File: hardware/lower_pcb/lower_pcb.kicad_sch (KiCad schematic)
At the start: 0 parts

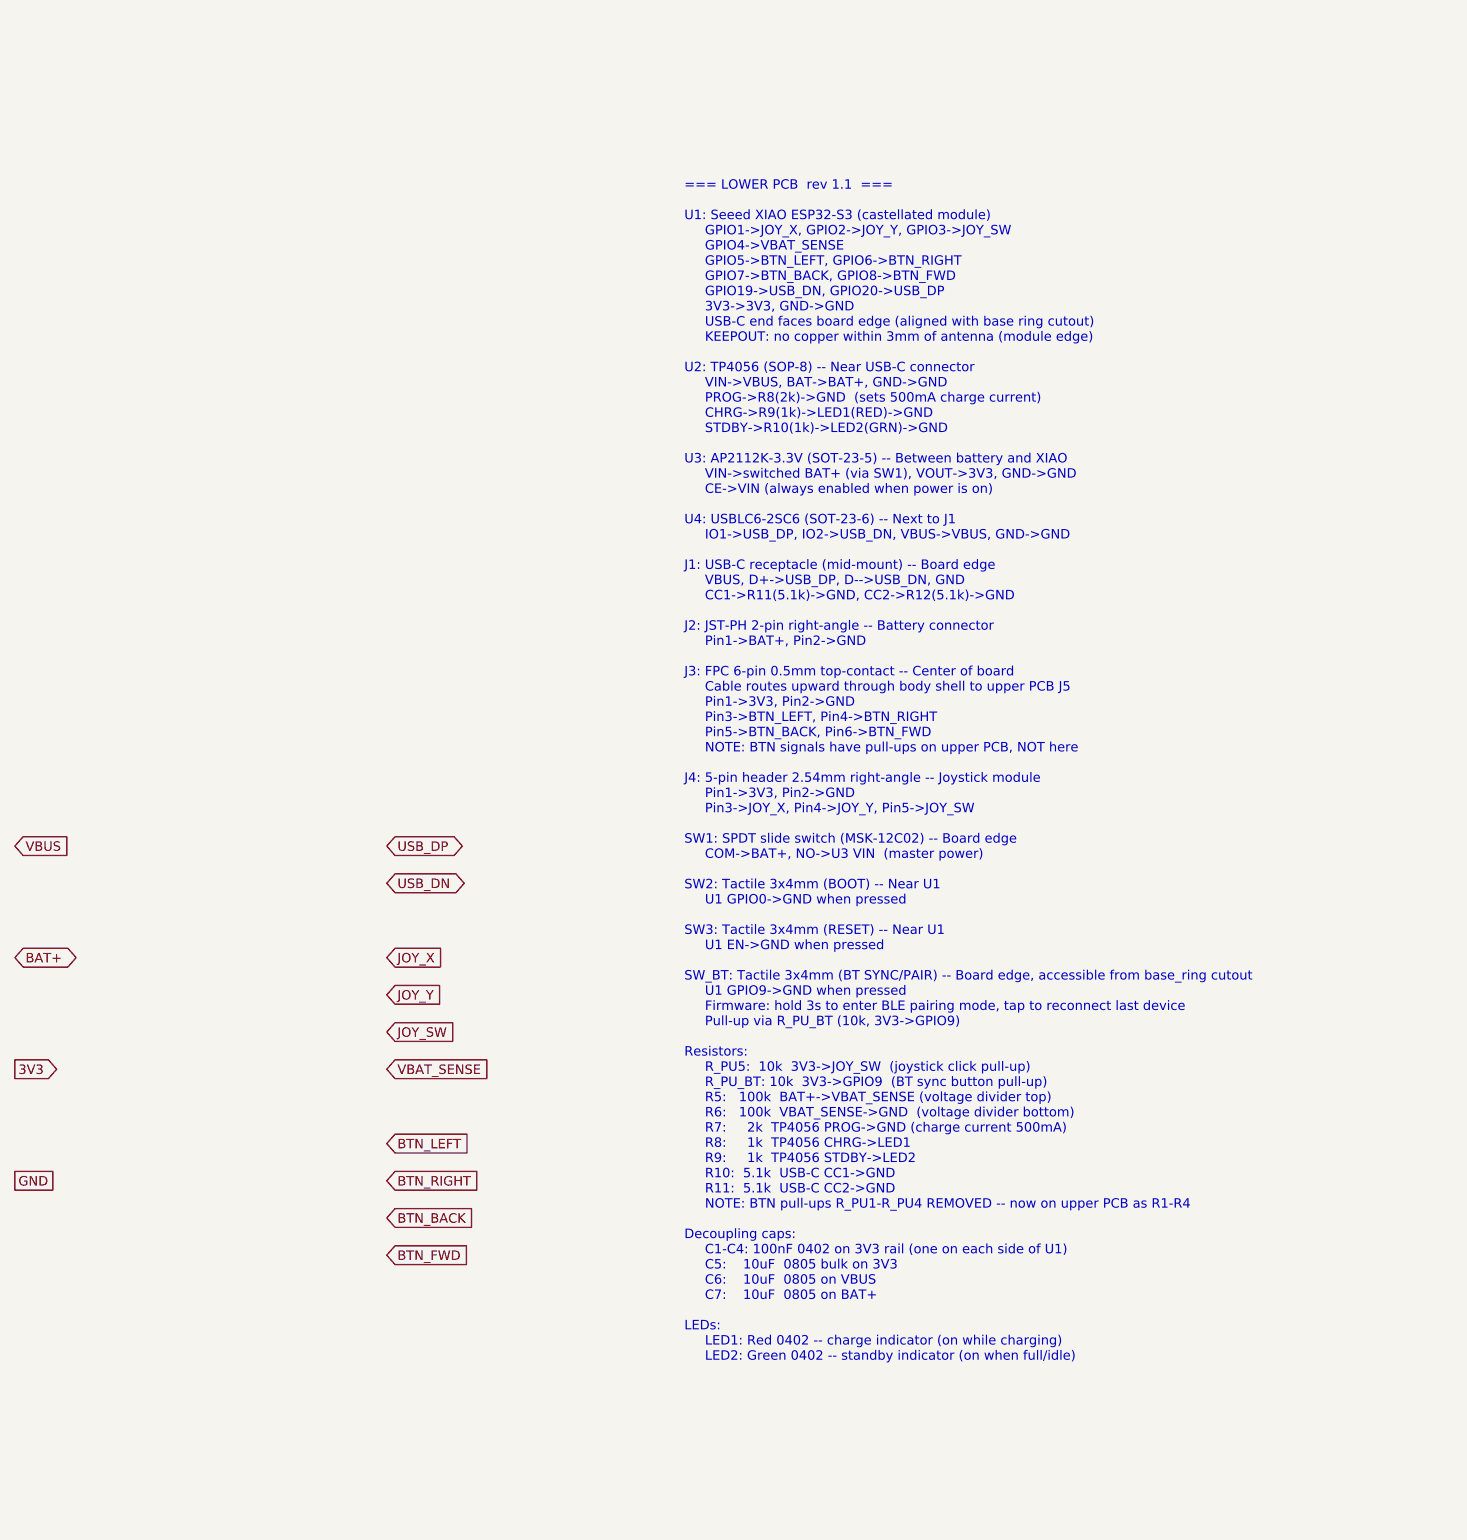
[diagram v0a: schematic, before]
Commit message: feat: lower PCB rev 2.0 - remove TP4056/USBLC6, use XIAO onboard charger+ADC
- REMOVED: U2 TP4056, U4 USBLC6, R5/R6 VBAT divider, R7/R8/R9, LED1/LED2
- XIAO ESP32-S3 handles LiPo charging (~100mA onboard), USB ESD, charge LED
- Battery ADC: GPIO10 (ADC_BAT) used directly - onboard voltage divider on XIAO
- GPIO4 reassigned (freed), GPIO10 = ADC_BAT
- Silkscreen updated: G10-ADC-BAT label, U2/U4/LED silk removed
- Simplified BOM: 8 fewer components, ~3 USD savings per unit
- docs/BOM.md updated with corrected parts list
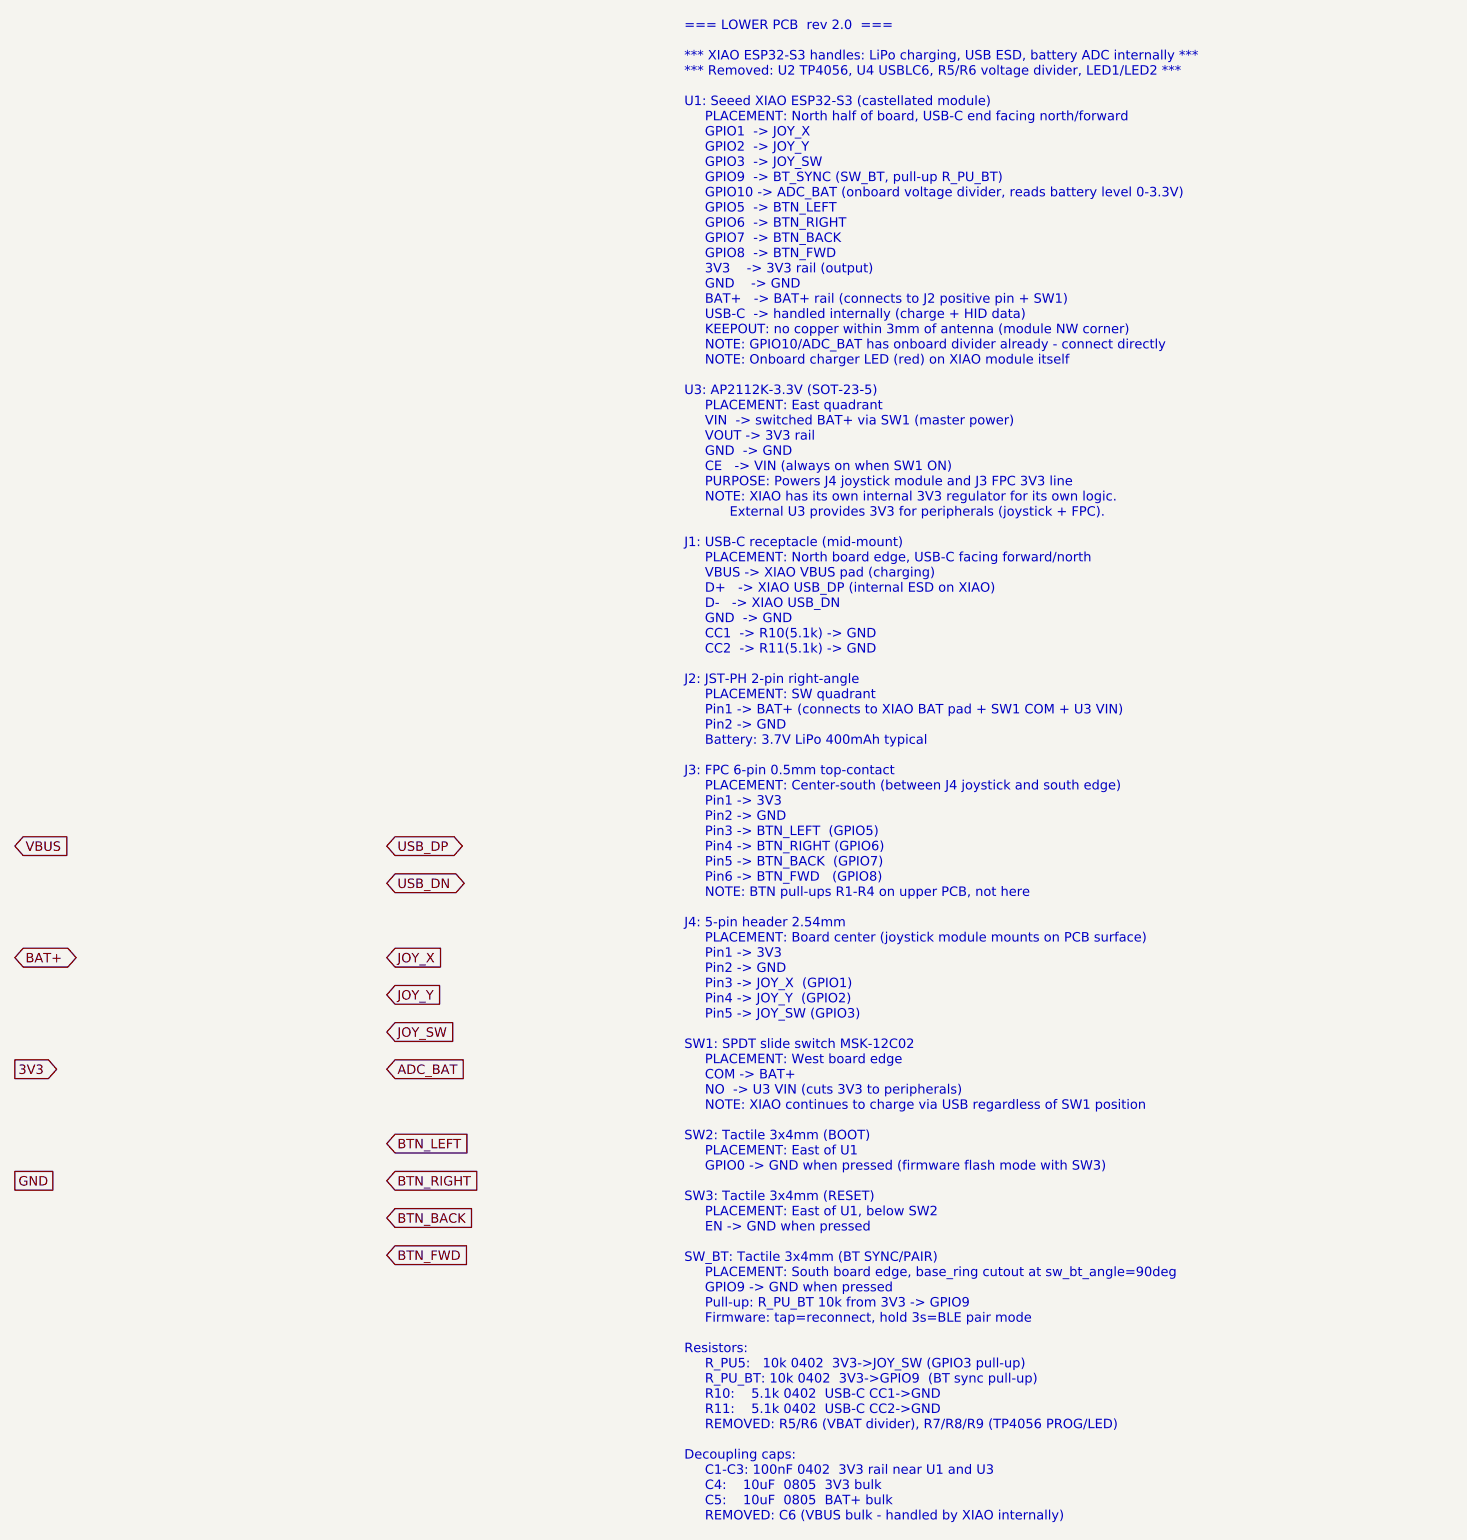
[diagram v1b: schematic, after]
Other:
- note added: "=== LOWER PCB rev 2.0 === *** XIAO ESP32-S3 handles: LiPo charging, USB ESD, battery ADC internally *** *** Removed: U2 TP4056, U4 USBLC6, R5/R6 voltage divider, LED1/LED2 *** U1: Seeed XIAO ESP32-S3 (castellated module) PLACEMENT: North half of board, USB-C end facing north/forward GPIO1 -> JOY_X GPIO2 -> JOY_Y GPIO3 -> JOY_SW GPIO9 -> BT_SYNC (SW_BT, pull-up R_PU_BT) GPIO10 -> ADC_BAT (onboard 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"
- note removed: "=== LOWER PCB rev 1.1 === U1: Seeed XIAO ESP32-S3 (castellated module) GPIO1->JOY_X, GPIO2->JOY_Y, GPIO3->JOY_SW GPIO4->VBAT_SENSE GPIO5->BTN_LEFT, GPIO6->BTN_RIGHT GPIO7->BTN_BACK, GPIO8->BTN_FWD GPIO19->USB_DN, GPIO20->USB_DP 3V3->3V3, GND->GND USB-C end faces board edge (aligned with base ring cutout) KEEPOUT: no copper within 3mm of antenna (module edge) U2: TP4056 (SOP-8) -- Near USB-C conne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"
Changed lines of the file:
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@@
   (title_block
     (title "DaPao Space Mouse - Lower PCB")
-    (date "2026-03-20")
-    (rev "1.1")
+    (date "2026-03-21")
+    (rev "2.0")
     (comment 1 "Base board: XIAO ESP32-S3 + Power + Joystick + FPC")
     (comment 2 "Circular PCB dia88mm, 2-layer, 1.6mm thick")
-    (comment 3 "Rev 1.1: BTN pull-ups moved to upper PCB (R1-R4). R_PU5 (JOY_SW) stays here.")
+    (comment 3 "Rev 2.0: Removed TP4056/USBLC6/voltage divider - XIAO handles charging, ESD, BAT ADC internally")
+    (comment 4 "XIAO onboard charger ~100mA via USB-C. BAT voltage on GPIO10 (ADC_BAT). BAT+ wired to XIAO BAT pad.")
   )
   ;; --- POWER NETS ---
-  (global_label "VBUS" (shape input) (at 30 40 0)
-    (effects (font (size 1.27 1.27)))
-  )
-  (global_label "BAT+" (shape bidirectional) (at 30 55 0)
-    (effects (font (size 1.27 1.27)))
-  )
-  (global_label "3V3" (shape output) (at 30 70 0)
-    (effects (font (size 1.27 1.27)))
-  )
-  (global_label "GND" (shape passive) (at 30 85 0)
-    (effects (font (size 1.27 1.27)))
-  )
+  (global_label "VBUS"  (shape input)        (at 30 40 0) (effects (font (size 1.27 1.27))))
+  (global_label "BAT+"  (shape bidirectional) (at 30 55 0) (effects (font (size 1.27 1.27))))
+  (global_label "3V3"   (shape output)        (at 30 70 0) (effects (font (size 1.27 1.27))))
+  (global_label "GND"   (shape passive)       (at 30 85 0) (effects (font (size 1.27 1.27))))
   ;; --- SIGNAL NETS ---
-  (global_label "USB_DP"     (shape bidirectional) (at 80 40 0) (effects (font (size 1.27 1.27))))
-  (global_label "USB_DN"     (shape bidirectional) (at 80 45 0) (effects (font (size 1.27 1.27))))
-  (global_label "JOY_X"      (shape input) (at 80 55 0) (effects (font (size 1.27 1.27))))
-  (global_label "JOY_Y"      (shape input) (at 80 60 0) (effects (font (size 1.27 1.27))))
-  (global_label "JOY_SW"     (shape input) (at 80 65 0) (effects (font (size 1.27 1.27))))
-  (global_label "VBAT_SENSE" (shape input) (at 80 70 0) (effects (font (size 1.27 1.27))))
-  (global_label "BTN_LEFT"   (shape input) (at 80 80 0) (effects (font (size 1.27 1.27))))
-  (global_label "BTN_RIGHT"  (shape input) (at 80 85 0) (effects (font (size 1.27 1.27))))
-  (global_label "BTN_BACK"   (shape input) (at 80 90 0) (effects (font (size 1.27 1.27))))
-  (global_label "BTN_FWD"    (shape input) (at 80 95 0) (effects (font (size 1.27 1.27))))
+  (global_label "USB_DP"    (shape bidirectional) (at 80 40 0) (effects (font (size 1.27 1.27))))
+  (global_label "USB_DN"    (shape bidirectional) (at 80 45 0) (effects (font (size 1.27 1.27))))
+  (global_label "JOY_X"     (shape input)         (at 80 55 0) (effects (font (size 1.27 1.27))))
+  (global_label "JOY_Y"     (shape input)         (at 80 60 0) (effects (font (size 1.27 1.27))))
+  (global_label "JOY_SW"    (shape input)         (at 80 65 0) (effects (font (size 1.27 1.27))))
+  (global_label "ADC_BAT"   (shape input)         (at 80 70 0) (effects (font (size 1.27 1.27))))
+  (global_label "BTN_LEFT"  (shape input)         (at 80 80 0) (effects (font (size 1.27 1.27))))
+  (global_label "BTN_RIGHT" (shape input)         (at 80 85 0) (effects (font (size 1.27 1.27))))
+  (global_label "BTN_BACK"  (shape input)         (at 80 90 0) (effects (font (size 1.27 1.27))))
+  (global_label "BTN_FWD"   (shape input)         (at 80 95 0) (effects (font (size 1.27 1.27))))
   ;; --- COMPONENT PLACEMENT & WIRING NOTES ---
-  (text "=== LOWER PCB  rev 1.1  ===\n\nU1: Seeed XIAO ESP32-S3 (castellated module)\n     GPIO1->JOY_X, GPIO2->JOY_Y, GPIO3->JOY_SW\n     GPIO4->VBAT_SENSE\n     GPIO5->BTN_LEFT, GPIO6->BTN_RIGHT\n     GPIO7->BTN_BACK, GPIO8->BTN_FWD\n     GPIO19->USB_DN, GPIO20->USB_DP\n     3V3->3V3, GND->GND\n     USB-C end faces board edge (aligned with base ring cutout)\n     KEEPOUT: no copper within 3mm of antenna (module edge)\n\nU2: TP4056 (SOP-8) -- Near USB-C connector\n     VIN->VBUS, BAT->BAT+, GND->GND\n     PROG->R8(2k)->GND  (sets 500mA charge current)\n     CHRG->R9(1k)->LED1(RED)->GND\n     STDBY->R10(1k)->LED2(GRN)->GND\n\nU3: AP2112K-3.3V (SOT-23-5) -- Between battery and XIAO\n     VIN->switched BAT+ (via SW1), VOUT->3V3, GND->GND\n     CE->VIN (always enabled when power is on)\n\nU4: USBLC6-2SC6 (SOT-23-6) -- Next to J1\n     IO1->USB_DP, IO2->USB_DN, VBUS->VBUS, GND->GND\n\nJ1: USB-C receptacle (mid-mount) -- Board edge\n     VBUS, D+->USB_DP, D-->USB_DN, GND\n     CC1->R11(5.1k)->GND, CC2->R12(5.1k)->GND\n\nJ2: JST-PH 2-pin right-angle -- Battery connector\n     Pin1->BAT+, Pin2->GND\n\nJ3: FPC 6-pin 0.5mm top-contact -- Center of board\n     Cable routes upward through body shell to upper PCB J5\n     Pin1->3V3, Pin2->GND\n     Pin3->BTN_LEFT, Pin4->BTN_RIGHT\n     Pin5->BTN_BACK, Pin6->BTN_FWD\n     NOTE: BTN signals have pull-ups on upper PCB, NOT here\n\nJ4: 5-pin header 2.54mm right-angle -- Joystick module\n     Pin1->3V3, Pin2->GND\n     Pin3->JOY_X, Pin4->JOY_Y, Pin5->JOY_SW\n\nSW1: SPDT slide switch (MSK-12C02) -- Board edge\n     COM->BAT+, NO->U3 VIN  (master power)\n\nSW2: Tactile 3x4mm (BOOT) -- Near U1\n     U1 GPIO0->GND when pressed\n\nSW3: Tactile 3x4mm (RESET) -- Near U1\n     U1 EN->GND when pressed\n\nSW_BT: Tactile 3x4mm (BT SYNC/PAIR) -- Board edge, accessible from base_ring cutout\n     U1 GPIO9->GND when pressed\n     Firmware: hold 3s to enter BLE pairing mode, tap to reconnect last device\n     Pull-up via R_PU_BT (10k, 3V3->GPIO9)\n\nResistors:\n     R_PU5:  10k  3V3->JOY_SW  (joystick click pull-up)\n     R_PU_BT: 10k  3V3->GPIO9  (BT sync button pull-up)\n     R5:   100k  BAT+->VBAT_SENSE (voltage divider top)\n     R6:   100k  VBAT_SENSE->GND  (voltage divider bottom)\n     R7:     2k  TP4056 PROG->GND (charge current 500mA)\n     R8:     1k  TP4056 CHRG->LED1\n     R9:     1k  TP4056 STDBY->LED2\n     R10:  5.1k  USB-C CC1->GND\n     R11:  5.1k  USB-C CC2->GND\n     NOTE: BTN pull-ups R_PU1-R_PU4 REMOVED -- now on upper PCB as R1-R4\n\nDecoupling caps:\n     C1-C4: 100nF 0402 on 3V3 rail (one on each side of U1)\n     C5:    10uF  0805 bulk on 3V3\n     C6:    10uF  0805 on VBUS\n     C7:    10uF  0805 on BAT+\n\nLEDs:\n     LED1: Red 0402 -- charge indicator (on while charging)\n     LED2: Green 0402 -- standby indicator (on when full/idle)"
+  (text "=== LOWER PCB  rev 2.0  ===\n\n*** XIAO ESP32-S3 handles: LiPo charging, USB ESD, battery ADC internally ***\n*** Removed: U2 TP4056, U4 USBLC6, R5/R6 voltage divider, LED1/LED2 ***\n\nU1: Seeed XIAO ESP32-S3 (castellated module)\n     PLACEMENT: North half of board, USB-C end facing north/forward\n     GPIO1  -> JOY_X\n     GPIO2  -> JOY_Y\n     GPIO3  -> JOY_SW\n     GPIO9  -> BT_SYNC (SW_BT, pull-up R_PU_BT)\n     GPIO10 -> ADC_BAT (onboard voltage divider, reads battery level 0-3.3V)\n     GPIO5  -> BTN_LEFT\n     GPIO6  -> BTN_RIGHT\n     GPIO7  -> BTN_BACK\n     GPIO8  -> BTN_FWD\n     3V3    -> 3V3 rail (output)\n     GND    -> GND\n     BAT+   -> BAT+ rail (connects to J2 positive pin + SW1)\n     USB-C  -> handled internally (charge + HID data)\n     KEEPOUT: no copper within 3mm of antenna (module NW corner)\n     NOTE: GPIO10/ADC_BAT has onboard divider already - connect directly\n     NOTE: Onboard charger LED (red) on XIAO module itself\n\nU3: AP2112K-3.3V (SOT-23-5)\n     PLACEMENT: East quadrant\n     VIN  -> switched BAT+ via SW1 (master power)\n     VOUT -> 3V3 rail\n     GND  -> GND\n     CE   -> VIN (always on when SW1 ON)\n     PURPOSE: Powers J4 joystick module and J3 FPC 3V3 line\n     NOTE: XIAO has its own internal 3V3 regulator for its own logic.\n           External U3 provides 3V3 for peripherals (joystick + FPC).\n\nJ1: USB-C receptacle (mid-mount)\n     PLACEMENT: North board edge, USB-C facing forward/north\n     VBUS -> XIAO VBUS pad (charging)\n     D+   -> XIAO USB_DP (internal ESD on XIAO)\n     D-   -> XIAO USB_DN\n     GND  -> GND\n     CC1  -> R10(5.1k) -> GND\n     CC2  -> R11(5.1k) -> GND\n\nJ2: JST-PH 2-pin right-angle\n     PLACEMENT: SW quadrant\n     Pin1 -> BAT+ (connects to XIAO BAT pad + SW1 COM + U3 VIN)\n     Pin2 -> GND\n     Battery: 3.7V LiPo 400mAh typical\n\nJ3: FPC 6-pin 0.5mm top-contact\n     PLACEMENT: Center-south (between J4 joystick and south edge)\n     Pin1 -> 3V3\n     Pin2 -> GND\n     Pin3 -> BTN_LEFT  (GPIO5)\n     Pin4 -> BTN_RIGHT (GPIO6)\n     Pin5 -> BTN_BACK  (GPIO7)\n     Pin6 -> BTN_FWD   (GPIO8)\n     NOTE: BTN pull-ups R1-R4 on upper PCB, not here\n\nJ4: 5-pin header 2.54mm\n     PLACEMENT: Board center (joystick module mounts on PCB surface)\n     Pin1 -> 3V3\n     Pin2 -> GND\n     Pin3 -> JOY_X  (GPIO1)\n     Pin4 -> JOY_Y  (GPIO2)\n     Pin5 -> JOY_SW (GPIO3)\n\nSW1: SPDT slide switch MSK-12C02\n     PLACEMENT: West board edge\n     COM -> BAT+\n     NO  -> U3 VIN (cuts 3V3 to peripherals)\n     NOTE: XIAO continues to charge via USB regardless of SW1 position\n\nSW2: Tactile 3x4mm (BOOT)\n     PLACEMENT: East of U1\n     GPIO0 -> GND when pressed (firmware flash mode with SW3)\n\nSW3: Tactile 3x4mm (RESET)\n     PLACEMENT: East of U1, below SW2\n     EN -> GND when pressed\n\nSW_BT: Tactile 3x4mm (BT SYNC/PAIR)\n     PLACEMENT: South board edge, base_ring cutout at sw_bt_angle=90deg\n     GPIO9 -> GND when pressed\n     Pull-up: R_PU_BT 10k from 3V3 -> GPIO9\n     Firmware: tap=reconnect, hold 3s=BLE pair mode\n\nResistors:\n     R_PU5:   10k 0402  3V3->JOY_SW (GPIO3 pull-up)\n     R_PU_BT: 10k 0402  3V3->GPIO9  (BT sync pull-up)\n     R10:    5.1k 0402  USB-C CC1->GND\n     R11:    5.1k 0402  USB-C CC2->GND\n     REMOVED: R5/R6 (VBAT divider), R7/R8/R9 (TP4056 PROG/LED)\n\nDecoupling caps:\n     C1-C3: 100nF 0402  3V3 rail near U1 and U3\n     C4:    10uF  0805  3V3 bulk\n     C5:    10uF  0805  BAT+ bulk\n     REMOVED: C6 (VBUS bulk - handled by XIAO internally)"
     (at 120 30 0)
     (effects (font (size 1.27 1.27)) (justify left))
